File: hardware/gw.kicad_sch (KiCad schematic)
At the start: 19 parts, among them J1 USB_OTG, J2 Conn_01x04, U1 ESP-12F, U2 Ai-Thinker-Ra-02, U3 AMS1117-3.3

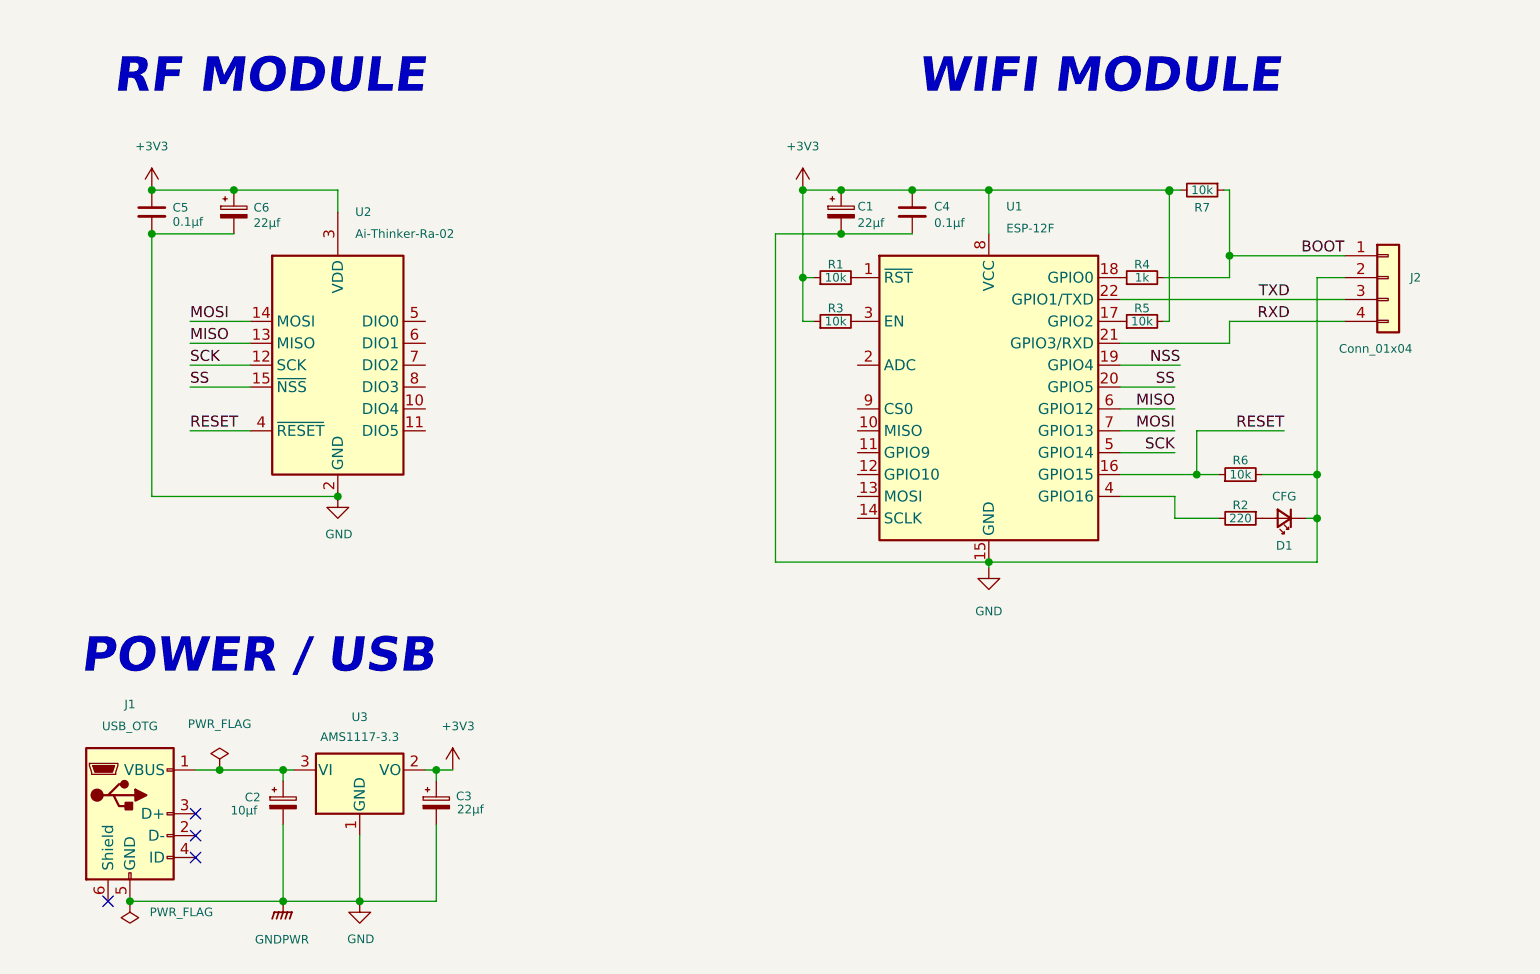
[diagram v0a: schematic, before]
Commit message: Add leds, fix layout
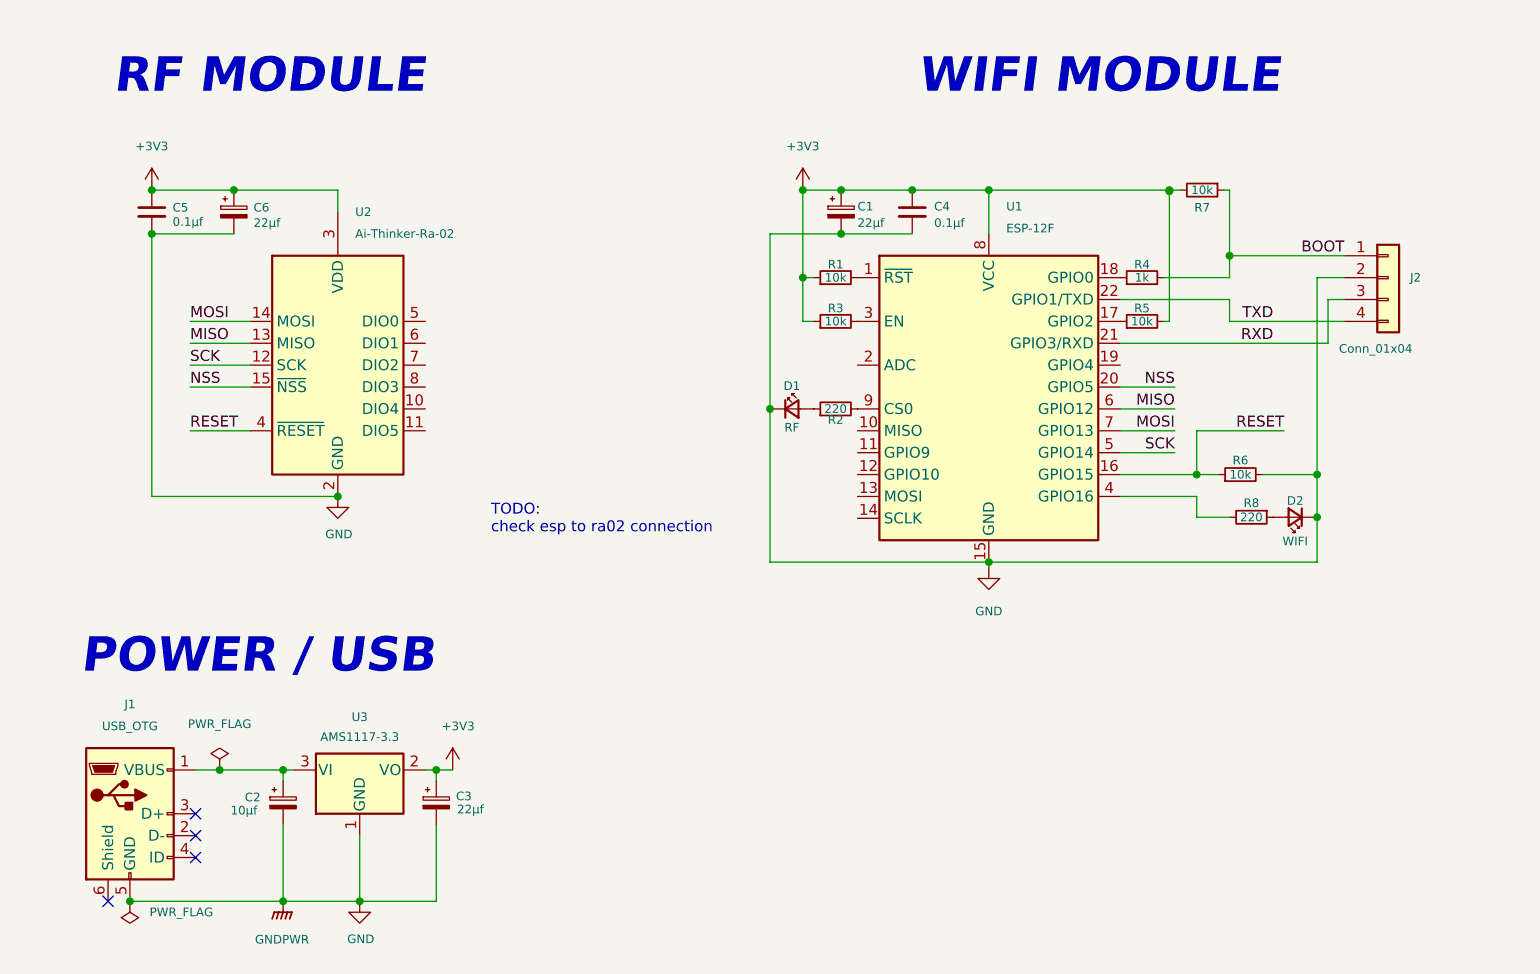
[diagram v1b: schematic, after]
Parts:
- added D2: WIFI, LED_SMD:LED_1206_3216Metric, symbol Device:LED_Small
- added R8: 220, Resistor_SMD:R_1206_3216Metric, symbol Device:R_Small
- D1: value CFG -> RF
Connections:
- net SS is gone; now on net NSS: U1.20 (GPIO5), U2.15 (~{NSS})
- net GND: now also D2.1 (K)
- net NSS: no longer U1.19 (GPIO4)
- net RXD: now also J2.3 (Pin_3); no longer J2.4 (Pin_4)
- net TXD: now also J2.4 (Pin_4); no longer J2.3 (Pin_3)
- net at R2.2: now also U1.9 (CS0); no longer U1.4 (GPIO16)
- new net: D2.2 (A), R8.1
- new net: R8.2, U1.4 (GPIO16)
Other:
- note added: "TODO: check esp to ra02 connection"
- moved on the sheet: D1, R2

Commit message: Update schematics, almost fab ready
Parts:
- U1: footprint RF_Module:ESP-12E -> RF_Module:ESP-07; symbol RF_Module:ESP-12F -> RF_Module:ESP-07
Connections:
- net GND: now also U1.9 (GND); no longer U1.15 (GND)
- net RESET: now also U1.10 (GPIO15); no longer U1.16 (GPIO15)
- net RXD: now also U1.15 (GPIO3/RXD); no longer U1.21 (GPIO3/RXD)
- net TXD: now also U1.16 (GPIO1/TXD); no longer U1.22 (GPIO1/TXD)
- net RF_LED: now reaches R2.2
- net RF_LED: now also U1.4 (GPIO16); no longer U1.9 (CS0)
- net WF_LED: now reaches R8.2
- net WF_LED: now also R4.1, U1.12 (GPIO0); no longer U1.4 (GPIO16)
- net DIO0: now reaches U2.5 (DIO0)
- net DIO0: now also R5.1, U1.11 (GPIO2)
- net DIO2: now reaches U2.7 (DIO2)
- net DIO2: now also U1.13 (GPIO4)
- net SS: now reaches U1.14 (GPIO5)
- net SS: now also U2.15 (~{NSS})
- removed net NSS: U1.20 (GPIO5), U2.15 (~{NSS})
- no-connect marks 4 -> 9
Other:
- note added: "STATUS LED"
- note added: "TODO: check esp to ra02 connection handle interrupt connection"
- note removed: "TODO: check esp to ra02 connection"
- moved on the sheet: C1, C4, C5, C6, D1, D2, J2, R1, R2, R3, R4, R5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

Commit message: Add DIO1 pin support
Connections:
- net RXD is gone; now on net DIO0: J2.3 (Pin_3), U1.15 (GPIO3/RXD)
- net DIO0: no longer R5.1, U1.11 (GPIO2)
- net DIO1: now reaches U2.6 (DIO1)
- net DIO1: now also R5.1, U1.11 (GPIO2)
- no-connect marks 9 -> 8
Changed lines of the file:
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@@
   (no_connect (at 40.64 112.395))
   (no_connect (at 40.64 117.475))
-  (no_connect (at 58.674 55.372))
   (no_connect (at 81.661 53.975))
   (no_connect (at 30.48 122.555))
@@
     (stroke (width 0) (type default) (color 0 0 0 0))
   )
-  (wire (pts (xy 112.141 51.435) (xy 120.904 51.435))
+  (wire (pts (xy 112.141 51.435) (xy 134.874 51.435))
     (stroke (width 0) (type default) (color 0 0 0 0))
   )
@@
   )
   (wire (pts (xy 127.508 43.815) (xy 133.223 43.815))
+    (stroke (width 0) (type default) (color 0 0 0 0))
+  )
+  (wire (pts (xy 58.674 55.372) (xy 63.627 55.372))
     (stroke (width 0) (type default) (color 0 0 0 0))
   )
@@
     (effects (font (size 1.27 1.27)) (justify left bottom))
   )
-  (label "DIO0" (at 120.904 48.895 180)
+  (label "DIO1" (at 120.904 48.895 180)
     (effects (font (size 1.27 1.27)) (justify right bottom))
   )
@@
     (effects (font (size 1.27 1.27)) (justify right bottom))
   )
+  (label "DIO0" (at 134.874 51.435 180)
+    (effects (font (size 1.27 1.27)) (justify right bottom))
+  )
   (label "SS" (at 120.904 56.515 180)
     (effects (font (size 1.27 1.27)) (justify right bottom))
@@
     (effects (font (size 1.27 1.27)) (justify left bottom))
   )
+  (label "DIO1" (at 63.627 55.372 180)
+    (effects (font (size 1.27 1.27)) (justify right bottom))
+  )
   (label "WF_LED" (at 120.904 43.815 180)

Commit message: Fix errors
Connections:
- net DIO0 renamed RXD_D0
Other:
- moved on the sheet: D1, D2, R2, R8

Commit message: Latest fixes
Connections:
- net DIO1 renamed DIO0
- net DIO0: now also U2.5 (DIO0); no longer U2.6 (DIO1)
- net RXD_D0 renamed RXD
- net RXD: no longer U2.5 (DIO0)
- no-connect marks 8 -> 9
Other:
- note added: "development references: https://github.com/kobuki/RFM69OOK https://github.com/jgromes/LoRaLib https://github.com/jgromes/RadioLib"
- note removed: "TODO: check esp to ra02 connection handle interrupt connection"
- moved on the sheet: C1, C4, D1, D2, R1, R2, R3, R4, R5, R6, R7, R8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

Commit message: Fixup pins
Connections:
- net DIO0: now also U1.14 (GPIO5); no longer R5.1, U1.11 (GPIO2)
- net SS: now also R5.1, U1.11 (GPIO2); no longer U1.14 (GPIO5)
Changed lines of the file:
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@@
     (effects (font (size 1.27 1.27)) (justify left bottom))
   )
-  (label "DIO0" (at 122.936 49.149 180)
+  (label "DIO0" (at 122.936 56.769 180)
     (effects (font (size 1.27 1.27)) (justify right bottom))
   )
@@
     (effects (font (size 1.27 1.27)) (justify right bottom))
   )
-  (label "SS" (at 122.936 56.769 180)
+  (label "SS" (at 122.936 49.149 180)
     (effects (font (size 1.27 1.27)) (justify right bottom))
   )

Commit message: Cleanup sch
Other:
- moved on the sheet: C1, C2, C3, C4, C5, C6, D1, D2, J1, J2, R1, R2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

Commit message: Latest prefab
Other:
- note added: "POWER | USB"
- note removed: "POWER / USB"
- moved on the sheet: C1, C4, R1, R3, R4, R5, R6, R7, U1
